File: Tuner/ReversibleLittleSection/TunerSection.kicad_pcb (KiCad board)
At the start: 2 copper layers, 100 x 100 mm, 113 parts, among them J1 Conn_01x03, J10 Conn_01x02, J11 Conn_02x05_Odd_Even, J12 Conn_01x01, J13 Conn_01x01, J14 Conn_01x01, J15 Conn_01x01, J2 Conn_01x03, J3 Conn_01x03, J4 Conn_01x03, J5 Conn_01x03, J6 Conn_01x03, J7 Conn_01x03, J8 Conn_01x02, J9 Conn_01x02, P10 Conn_01x01, P11 Conn_01x01, P12 Conn_01x01, P2 Conn_01x01, P3 Conn_01x01, P4 Conn_01x01, P5 Conn_01x01, P6 Conn_01x01, P7 Conn_01x01, P8 Conn_01x01, P9 Conn_01x01, U1 MCP23008, U2 ULN2803A

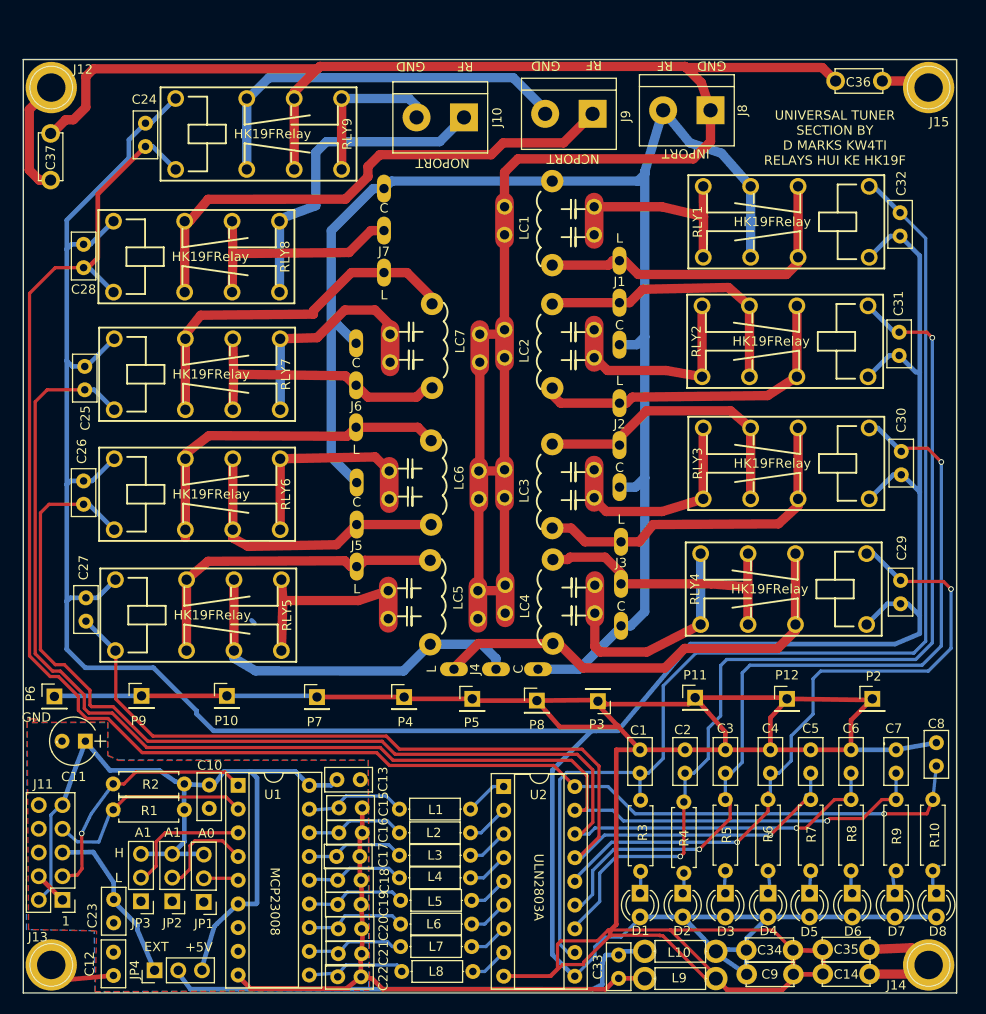
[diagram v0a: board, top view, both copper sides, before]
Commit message: Error in pinout HK19F fixed
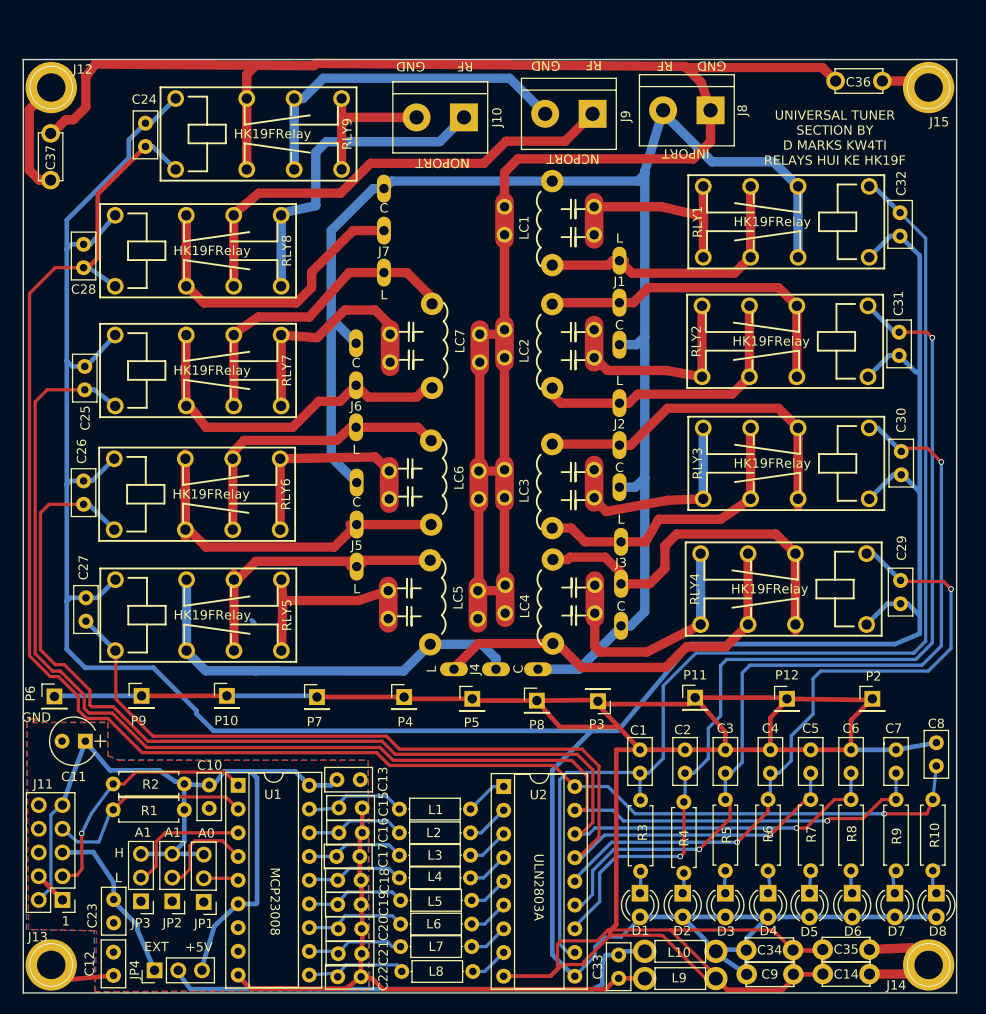
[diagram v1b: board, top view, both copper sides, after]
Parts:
- moved RLY8 0.66 mm to (62.2, 70.5)
- moved RLY7 0.42 mm to (62.2, 83.3)
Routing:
- net Net-(J3-Pad2): track 30.5 -> 42.0 mm
- net Net-(J7-Pad2): track 24.8 -> 33.7 mm
- net Net-(J6-Pad2): track 30.2 -> 38.4 mm
- net Net-(J5-Pad2): track 30.9 -> 38.6 mm
- net Net-(J6-Pad1): track 37.7 -> 31.2 mm
- net Net-(J2-Pad2): track 31.6 -> 38.0 mm
- net Net-(J9-Pad1): track 56.8 -> 50.5 mm
- net Net-(J7-Pad1): track 39.3 -> 33.4 mm
- net Net-(J1-Pad2): track 30.1 -> 35.8 mm
- net Net-(J3-Pad1): track 36.9 -> 31.5 mm
- net RFPORT1: track 162.7 -> 167.9 mm
- net Net-(J1-Pad1): track 35.9 -> 30.8 mm
- net Net-(J9-Pad2): track 42.4 -> 37.4 mm
- net Net-(J4-Pad1): track 48.8 -> 43.9 mm
- net Net-(J4-Pad2): track 39.8 -> 44.7 mm
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
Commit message: JLCPCB Nov 1 2018
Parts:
- removed C36, C37: 10 nF, Capacitors_THT:C_Disc_D5.0mm_W2.5mm_P5.00mm
- added J16: Conn_01x01, tuner:SOLDERJUMPER, F.Cu at (129.1, 52.1)
- added J17: Conn_01x01, tuner:SOLDERJUMPER, F.Cu at (88.7, 54.2)
- added J18: Conn_01x01, tuner:SOLDERJUMPER, F.Cu at (141.7, 51.5)
- added J19: Conn_01x01, tuner:SOLDERJUMPER, F.Cu at (138.8, 51.4)
- added J20: Conn_01x01, tuner:SOLDERJUMPER, F.Cu at (58.8, 52.2)
- added J21: Conn_01x01, tuner:SOLDERJUMPER, F.Cu at (61.6, 52.2)
- added J22: Conn_01x01, tuner:SOLDERJUMPER, F.Cu at (79.0, 52.1)
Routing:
- net RFGND: track 201.0 -> 167.0 mm
- net Net-(J12-Pad1): track 14.1 -> 9.29 mm
- net Net-(J15-Pad1): track 5.25 -> 8.59 mm
- net Net-(J22-Pad1): track 37.4 -> 40.1 mm
- net Net-(J10-Pad2): track 15.9 -> 18.2 mm
- net RLY4: track 75.3 -> 74.6 mm
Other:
- board text added: "UNIVERSAL TUNER SECTION BY D MARKS KW4TI RELAYS HUI KE HK19F HONGFA HDF2 OMRON G5V-2"
- board text removed: "UNIVERSAL TUNER SECTION BY D MARKS KW4TI RELAYS HUI KE HK19F"

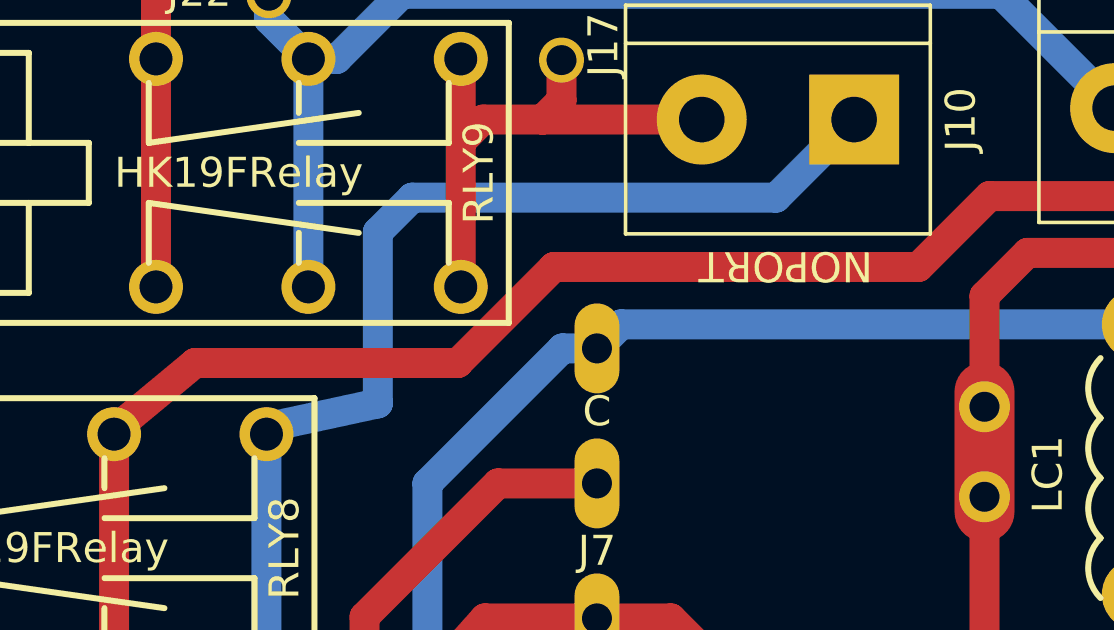
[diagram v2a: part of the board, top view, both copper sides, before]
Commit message: Added BNC and screw terminal combo pads
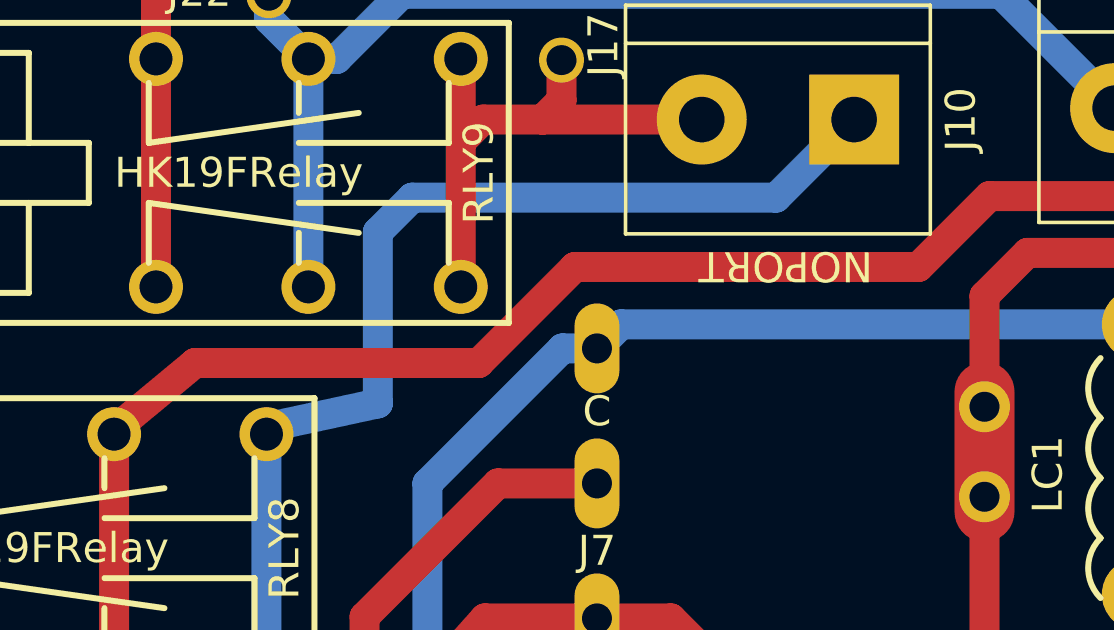
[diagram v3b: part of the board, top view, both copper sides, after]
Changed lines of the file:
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@@
   (segment (start 72.55 66.685) (end 72.55 66.5531) (width 1) (layer F.Cu) (net 24) (status 30))
   (segment (start 72.55 66.5531) (end 75.2475 64.3128) (width 1) (layer F.Cu) (net 24) (status 10))
-  (segment (start 75.2475 64.3128) (end 84.0105 64.3128) (width 1) (layer F.Cu) (net 24))
-  (segment (start 84.0105 64.3128) (end 87.2109 61.1124) (width 1) (layer F.Cu) (net 24))
-  (segment (start 87.2109 61.1124) (end 99.3648 61.1124) (width 1) (layer F.Cu) (net 24))
+  (segment (start 75.2475 64.3128) (end 84.709 64.3128) (width 1) (layer F.Cu) (net 24))
+  (segment (start 84.709 64.3128) (end 87.9094 61.1124) (width 1) (layer F.Cu) (net 24))
+  (segment (start 87.9094 61.1124) (end 99.3648 61.1124) (width 1) (layer F.Cu) (net 24))
   (segment (start 99.3648 61.1124) (end 101.727 58.7502) (width 1) (layer F.Cu) (net 24))
   (segment (start 101.727 58.7502) (end 108.0643 58.7502) (width 1) (layer F.Cu) (net 24))

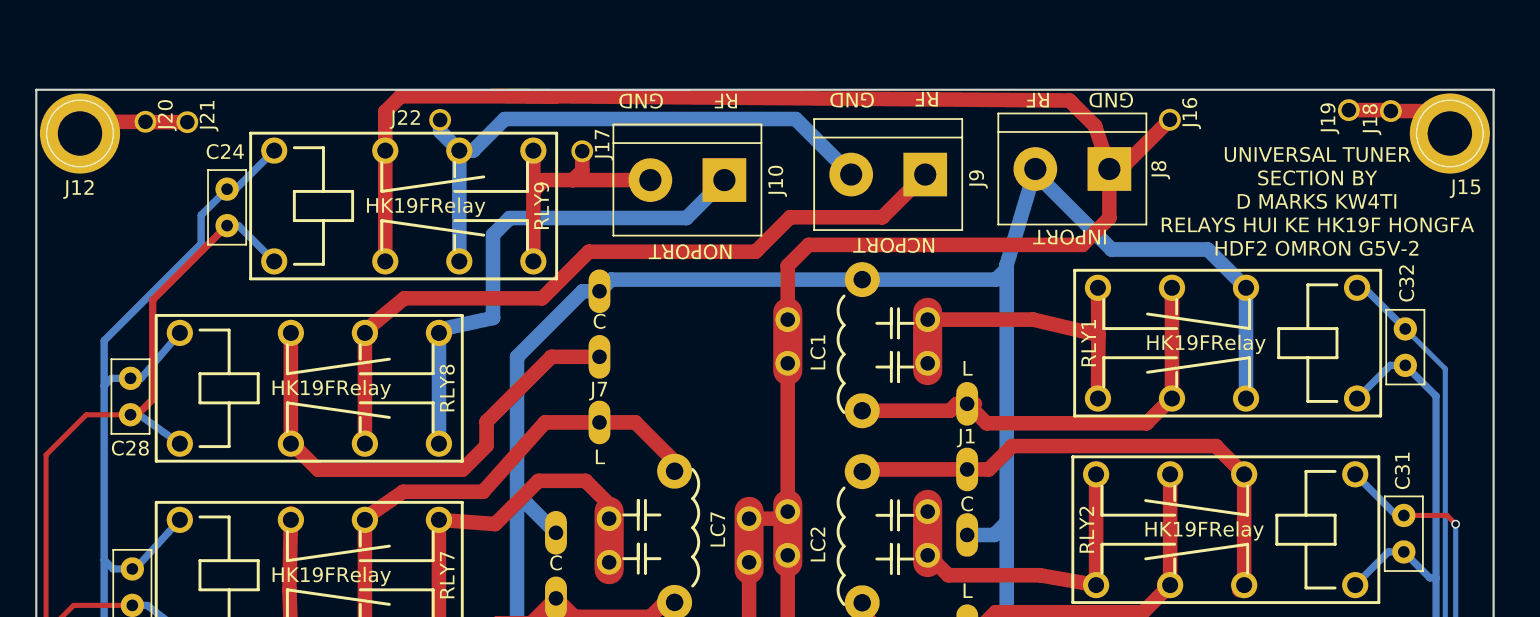
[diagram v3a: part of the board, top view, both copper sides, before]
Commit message: Modified connectors on Reversible boards
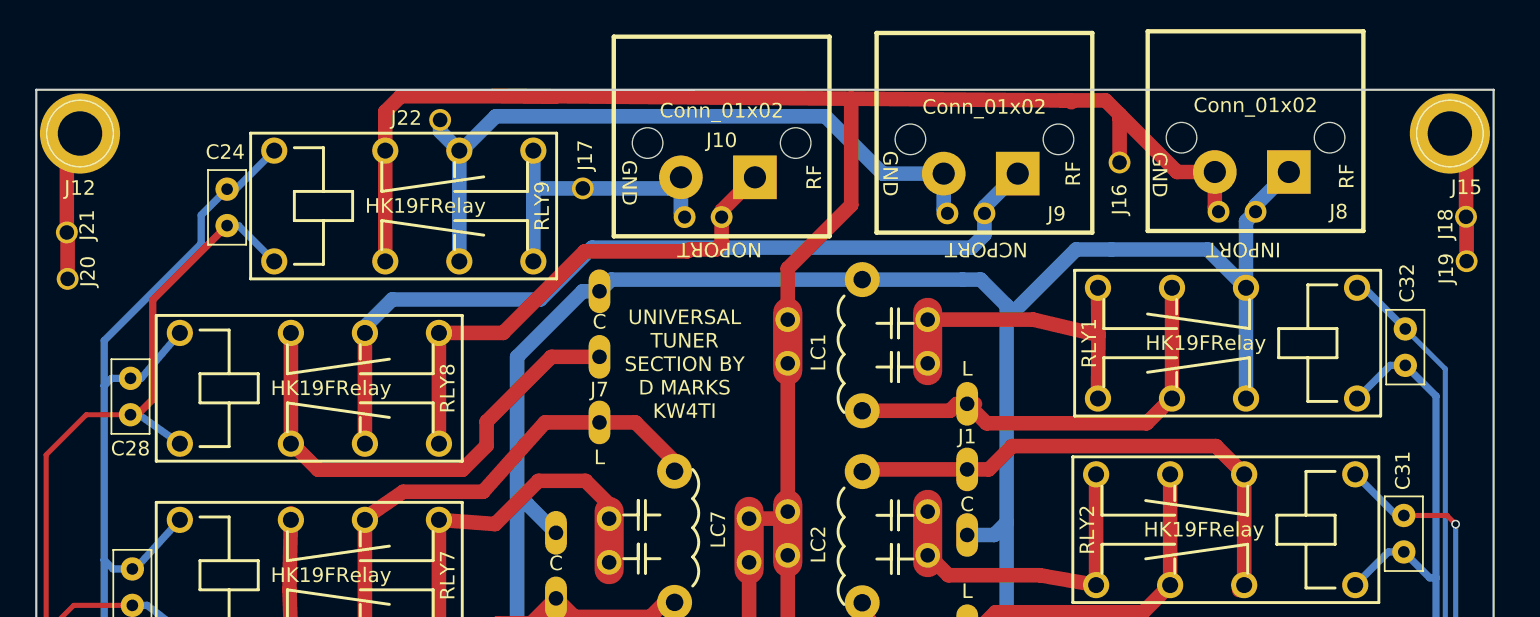
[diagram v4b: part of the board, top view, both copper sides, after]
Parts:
- J10, J8, J9: footprint Connectors_Terminal_Blocks:TerminalBlock_bornier-2_P5.08mm -> tuner:bnc_90_1-1337543-0_pad_combo
- moved J8 13.8 mm to (133.7, 46.0)
- moved J19 13.1 mm to (146.9, 61.8)
- moved J20 12.0 mm to (53.4, 63.0)
- moved J21 11.2 mm to (53.4, 59.8)
- moved J9 10.5 mm to (115.1, 46.1)
- moved J10 9.84 mm to (97.0, 46.4)
- moved J18 8.90 mm to (146.8, 58.7)
- moved J16 4.53 mm to (125.6, 55.0)
- moved J17 2.55 mm to (88.8, 56.8)
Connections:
- J8 pad 1: RFGND -> RFPORT1
- J8 pad 2: RFPORT1 -> RFGND
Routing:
- net Net-(J22-Pad1): track 40.1 -> 48.9 mm
- net Net-(J9-Pad1): track 50.5 -> 58.4 mm
- net RFGND: track 167.0 -> 161.7 mm
- net Net-(J12-Pad1): track 9.29 -> 13.5 mm
- net Net-(J15-Pad1): track 8.59 -> 12.4 mm
- net Net-(J10-Pad2): track 18.2 -> 20.9 mm
- net RFPORT1: track 167.9 -> 169.0 mm
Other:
- board text added: "UNIVERSAL TUNER SECTION BY D MARKS KW4TI"
- board text removed: "UNIVERSAL TUNER SECTION BY D MARKS KW4TI RELAYS HUI KE HK19F HONGFA HDF2 OMRON G5V-2"

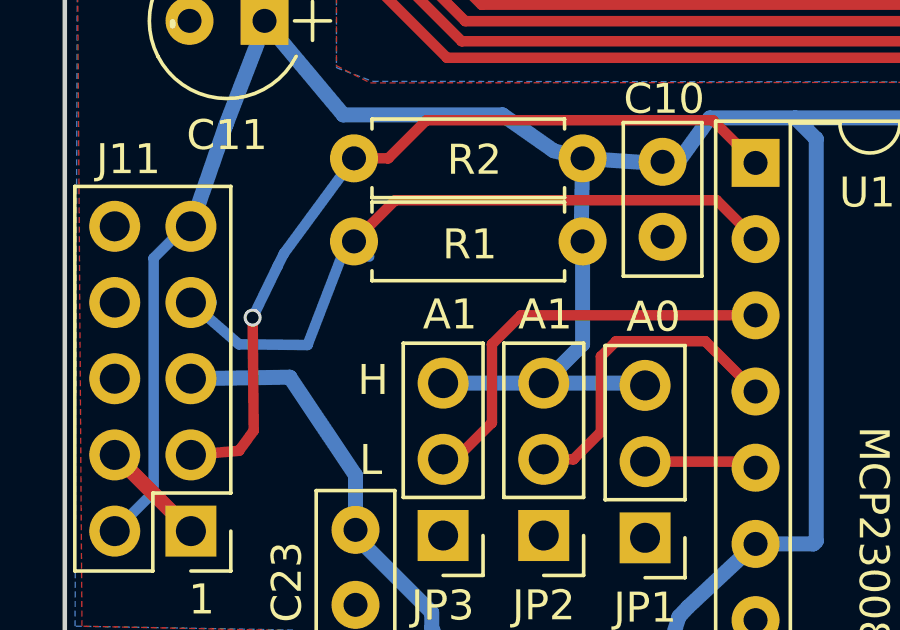
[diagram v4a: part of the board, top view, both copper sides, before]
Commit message: Symmetrized QuadCoupler Layout
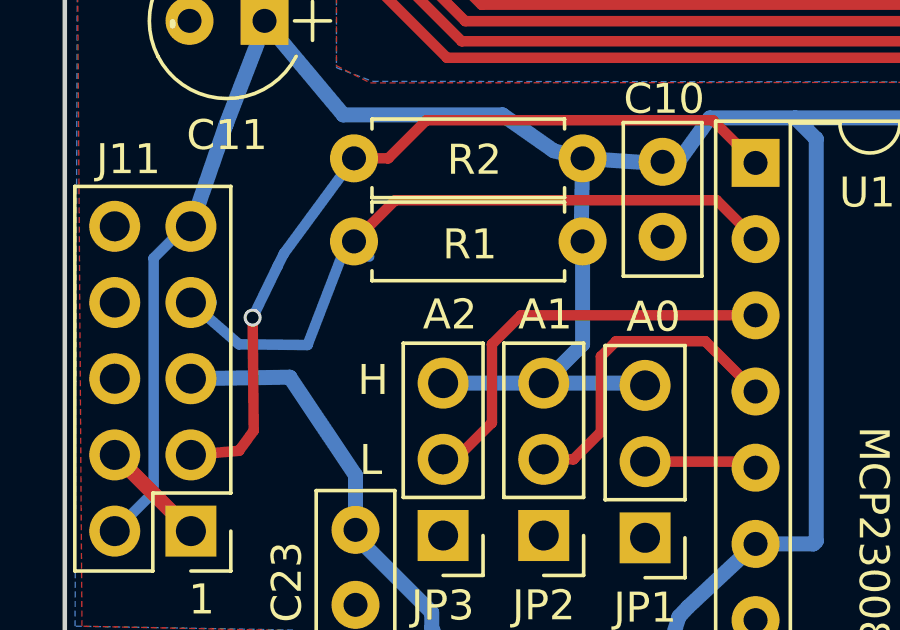
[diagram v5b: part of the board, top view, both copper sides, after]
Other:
- board text added: "A2"
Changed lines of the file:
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@@
     (effects (font (size 1 1) (thickness 0.15)))
   )
-  (gr_text A1 (at 62.8396 132.8166) (layer F.SilkS)
+  (gr_text A2 (at 62.8396 132.8166) (layer F.SilkS)
     (effects (font (size 1 1) (thickness 0.15)))
   )

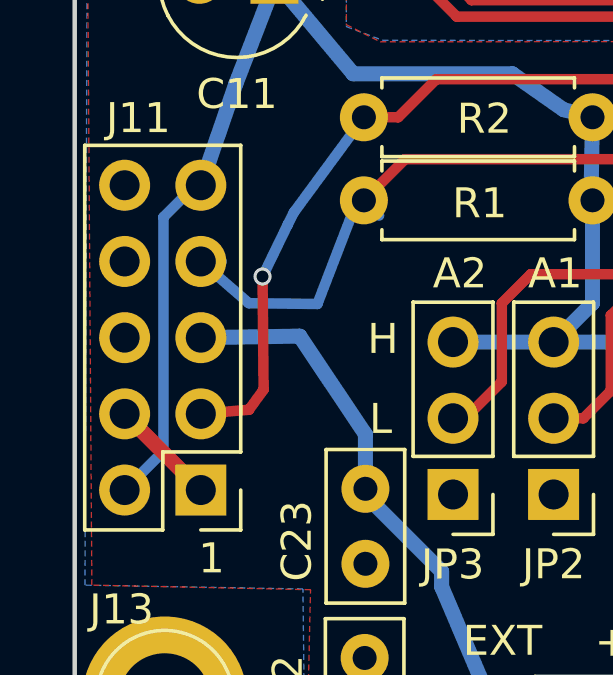
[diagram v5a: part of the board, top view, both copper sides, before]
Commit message: Changed I2C cable pinoutgit add Tunergit add Tuner Also added ICOM rig support
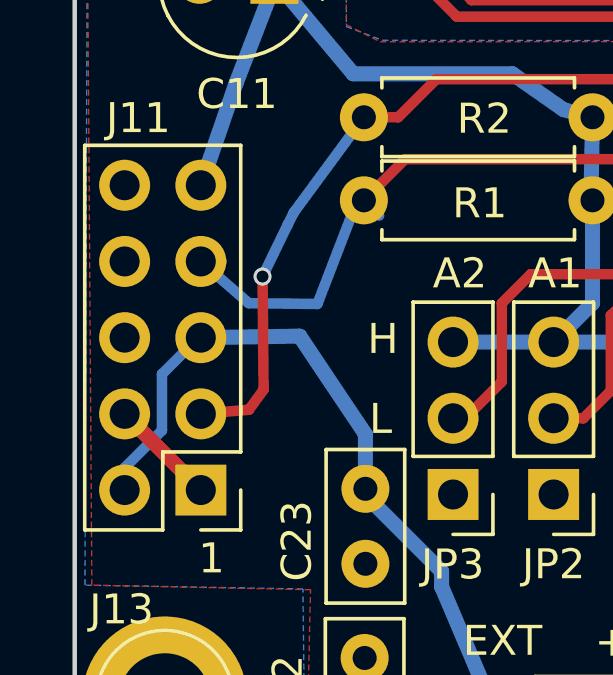
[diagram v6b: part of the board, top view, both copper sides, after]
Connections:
- J11 pad 2: +5V -> Net-(C23-Pad2)
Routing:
- net +5V: track 89.8 -> 78.2 mm
- net Net-(C23-Pad2): track 18.1 -> 24.7 mm
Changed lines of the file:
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@@
     (thickness 1.6)
     (drawings 27)
-    (tracks 882)
+    (tracks 884)
     (zones 0)
     (modules 118)
@@
   )
   (setup
-    (last_trace_width 0.25)
+    (last_trace_width 0.35)
     (user_trace_width 0.35)
     (user_trace_width 0.5)
@@
       (net 25 GND))
     (pad 2 thru_hole oval (at 2.54 0 180) (size 1.7 1.7) (drill 1) (layers *.Cu *.Mask)
-      (net 34 +5V))
+      (net 68 "Net-(C23-Pad2)"))
     (pad 3 thru_hole oval (at 0 2.54 180) (size 1.7 1.7) (drill 1) (layers *.Cu *.Mask)
       (net 69 SCL))
@@
   (segment (start 109.093 127.889) (end 109.347 127.889) (width 0.35) (layer F.Cu) (net 33) (status 30))
   (segment (start 54.2036 129.87528) (end 54.02072 129.87528) (width 0.35) (layer B.Cu) (net 34) (status 30))
-  (segment (start 54.02072 129.87528) (end 52.959 130.937) (width 0.35) (layer B.Cu) (net 34) (status 10))
-  (segment (start 52.959 138.73988) (end 51.6636 140.03528) (width 0.35) (layer B.Cu) (net 34) (status 20))
-  (segment (start 52.959 130.937) (end 52.959 138.73988) (width 0.35) (layer B.Cu) (net 34))
   (segment (start 73.025 140.462) (end 74.9554 140.462) (width 0.5) (layer B.Cu) (net 34) (status 10))
   (segment (start 75.04684 126.95936) (end 74.35088 126.2634) (width 0.5) (layer B.Cu) (net 34))
@@
   (segment (start 54.2036 129.87528) (end 55.372 126.492) (width 0.5) (layer B.Cu) (net 34) (status 10))
   (segment (start 55.372 126.492) (end 56.769 122.87504) (width 0.5) (layer B.Cu) (net 34) (status 20))
-  (segment (start 51.6636 140.03528) (end 51.6636 139.5603) (width 0.35) (layer B.Cu) (net 34) (status 30))
   (segment (start 56.769 122.87504) (end 56.769 123.12904) (width 1) (layer B.Cu) (net 34) (status 30))
   (segment (start 69.342 137.7188) (end 72.8218 137.7188) (width 0.35) (layer F.Cu) (net 35) (status 30))
@@
   (segment (start 146.0246 147.9804) (end 147.0025 147.0025) (width 1) (layer F.Cu) (net 67) (status 30))
   (segment (start 140.6652 147.9804) (end 140.6652 147.2184) (width 0.5) (layer F.Cu) (net 67) (status 30))
+  (segment (start 54.2036 134.95528) (end 54.12232 134.95528) (width 0.35) (layer B.Cu) (net 68))
+  (segment (start 54.12232 134.95528) (end 52.9082 136.1694) (width 0.35) (layer B.Cu) (net 68))
+  (segment (start 52.9082 138.049) (end 51.6636 139.2936) (width 0.35) (layer B.Cu) (net 68))
+  (segment (start 52.9082 136.1694) (end 52.9082 138.049) (width 0.35) (layer B.Cu) (net 68))
+  (segment (start 51.6636 139.2936) (end 51.6636 140.03528) (width 0.35) (layer B.Cu) (net 68))
+  (segment (start 51.6636 140.03528) (end 51.6636 139.5603) (width 0.35) (layer B.Cu) (net 68) (status 30))
   (segment (start 59.69 139.994) (end 59.69 140.208) (width 0.5) (layer B.Cu) (net 68) (status 30))
   (segment (start 59.69 140.208) (end 62.23 142.748) (width 0.5) (layer B.Cu) (net 68) (status 10))

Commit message: JLCPCB order 2019-03-25
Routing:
- net GND: track 68.0 -> 231.8 mm, vias 0 -> 28
